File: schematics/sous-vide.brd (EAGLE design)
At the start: 81.3 x 81.3 mm, 32 parts, among them IC1 MEGA8-P, T1 BC547, T2 BC547, T3 BC547

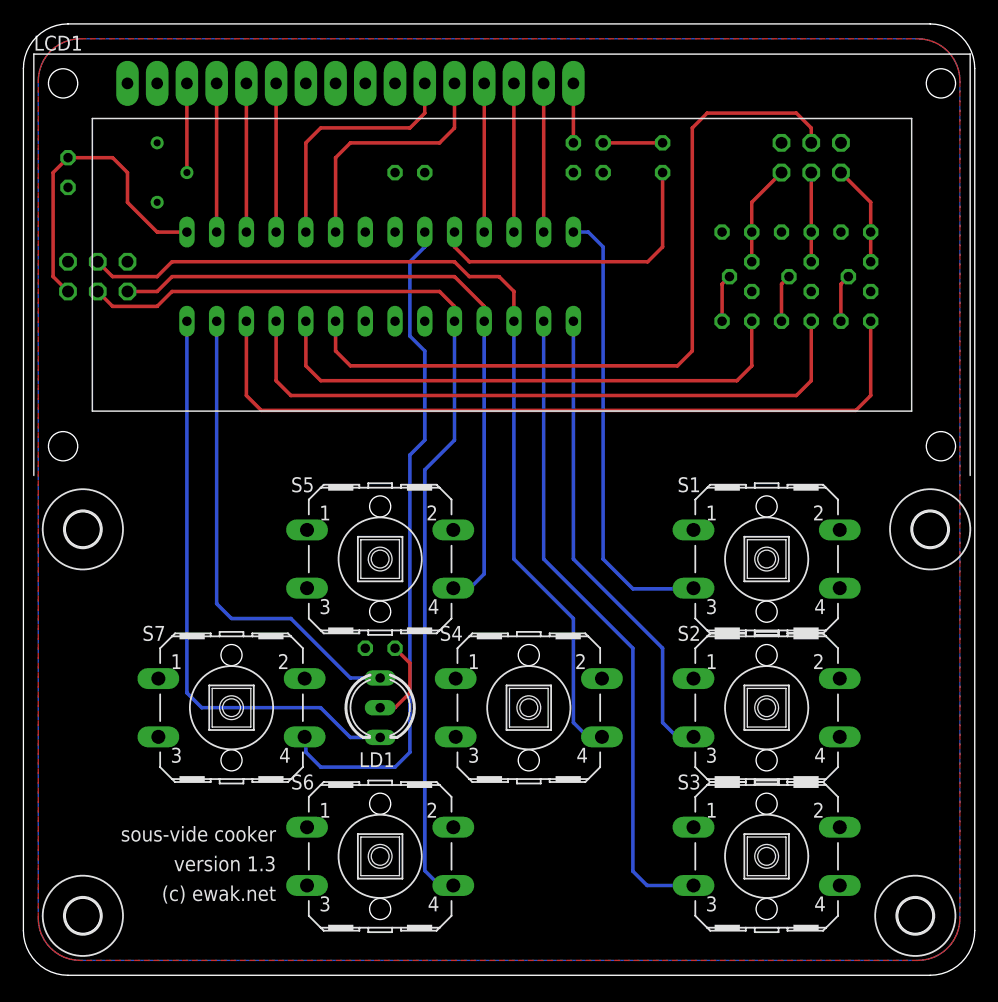
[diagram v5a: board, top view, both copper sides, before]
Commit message: Removed button and LED and added crystal for more precise timing over longer periods.
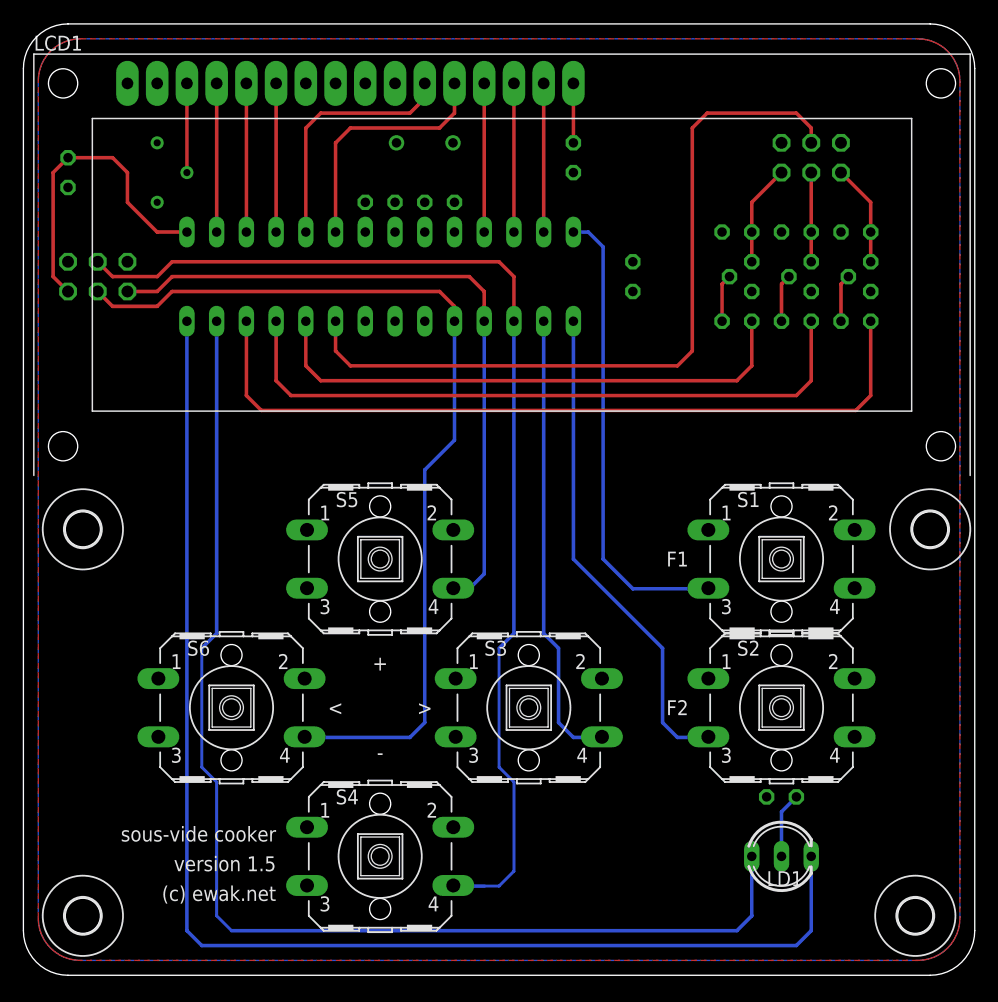
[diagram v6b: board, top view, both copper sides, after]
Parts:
- removed LED1: (no value), led:LED3MM
- removed R8: 180, rcl:0207/2V
- removed S7: (no value), switch-omron:B3F-40XX
- added C2, C3: 100n, resistor:C025-025X050
- added Q1: (no value), crystal:HC49U-V
- moved LD1 36.6 mm to (64.8, 10.2), turned to 0 degrees
- moved R7 36.6 mm to (64.8, 15.2)
- moved S3 24.0 mm to (43.2, 22.9)
- moved S4 18.0 mm to (30.5, 10.2)
- moved S6 18.0 mm to (17.8, 22.9)
- moved C1 3.59 mm to (30.5, 66.0), turned to 180 degrees
- moved S1 1.27 mm to (64.8, 35.6)
- moved S2 1.27 mm to (64.8, 22.9)
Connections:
- removed net N$26: IC1.9, S7.4
- net GND: now also C1.1, C2.1, C3.2; no longer C1.2, R8.1, S7.1, S7.2
- net N$1: now also C1.2, IC1.9, Q1.2; no longer LED1.K, R8.2
- net N$15: now also C2.2, Q1.1; no longer LED1.A
- net N$35: now also S3.4; no longer S3.3
- net VCC: now also C3.1; no longer C1.1
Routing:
- net N$8: track 49.8 -> 112.8 mm
- net N$9: track 40.7 -> 103.7 mm
- net N$26: track 57.3 -> 0.00 mm
- net N$15: track 26.5 -> 0.00 mm
- net N$35: track 55.8 -> 39.1 mm
- net N$24: track 79.6 -> 94.6 mm
- net N$1: track 5.08 -> 0.00 mm
- net N$18: track 83.1 -> 79.6 mm
- net N$19: track 58.0 -> 60.1 mm
- net N$7: track 7.40 -> 5.61 mm
- net N$37: track 40.6 -> 41.9 mm
- net N$36: track 38.5 -> 39.8 mm
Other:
- board text added: "+"
- board text added: "+S-"
- board text added: "-"
- board text added: "<"
- board text added: ">"
- board text added: "CONTRAST"
- board text added: "F1"
- board text added: "F2"
- board text added: "ISP"
- board text added: "PHC"
- board text added: "version 1.5"
- board text removed: "version 1.3"

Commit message: PCB button and connector layout rearranged. NOT COMPATIBEL WITH PRE-1.5 CODE.
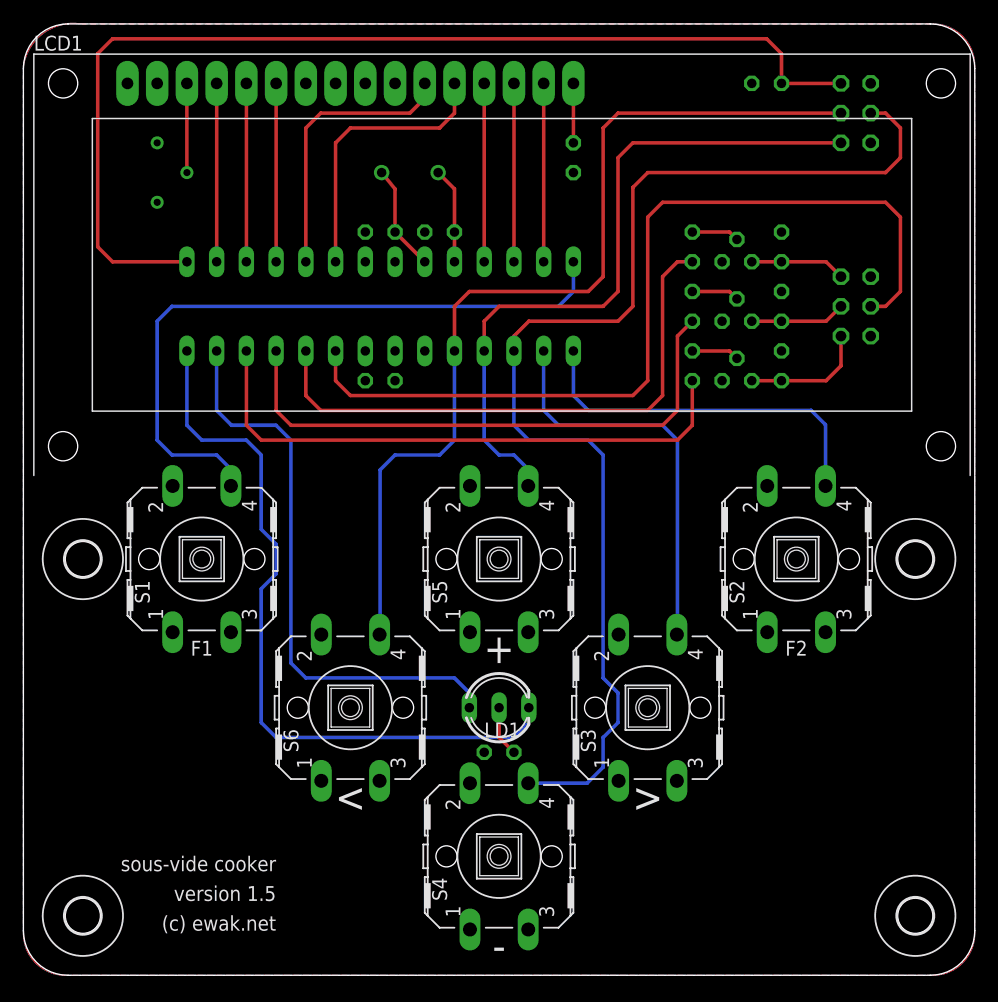
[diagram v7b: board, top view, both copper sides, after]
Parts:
- JP1, JP2: device pinhead:2X03 -> con-ml:ML6
- moved JP2 66.3 mm to (71.1, 73.7), turned to 90 degrees
- moved R1 60.2 mm to (63.5, 76.2), turned to 180 degrees
- moved S1 49.5 mm to (15.2, 35.6), turned to 90 degrees
- moved LD1 27.3 mm to (40.6, 22.9)
- moved R7 24.4 mm to (40.6, 19.1)
- moved C3 23.3 mm to (30.5, 50.8), turned to 0 degrees
- moved R4 14.5 mm to (57.1, 52.1), turned to 90 degrees
- moved T3 14.5 mm to (61.0, 50.8), turned to 0 degrees
- moved JP1 13.3 mm to (71.1, 57.1), turned to 90 degrees
- moved D3 13.1 mm to (64.8, 52.1), turned to 270 degrees
- moved S2 12.8 mm to (66.0, 35.6), turned to 90 degrees
- moved S3 10.2 mm to (53.3, 22.9), turned to 90 degrees
- moved S4 10.2 mm to (40.6, 10.2), turned to 90 degrees
- moved S5 10.2 mm to (40.6, 35.6), turned to 90 degrees
- moved S6 10.2 mm to (27.9, 22.9), turned to 90 degrees
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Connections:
- net N$36: now also S1.4; no longer S1.3
- net N$37: now also S2.4; no longer S2.3
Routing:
- net N$31: track 26.8 -> 91.7 mm
- net N$9: track 103.7 -> 49.1 mm
- net N$8: track 112.8 -> 62.8 mm
- net N$36: track 39.8 -> 58.1 mm
- net N$6: track 67.1 -> 49.3 mm
- net N$3: track 65.6 -> 76.3 mm
- net N$37: track 41.9 -> 31.6 mm
- net N$1: track 0.00 -> 9.08 mm
- net N$5: track 56.9 -> 48.6 mm
- net N$15: track 0.00 -> 8.20 mm
- net N$24: track 94.6 -> 101.9 mm
- net N$35: track 39.1 -> 34.2 mm
- net N$34: track 12.7 -> 15.2 mm
- net N$33: track 12.7 -> 15.2 mm
- net N$32: track 12.7 -> 15.2 mm
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
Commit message: Optimized traces and button definitions and send to pcb production as version 1.5
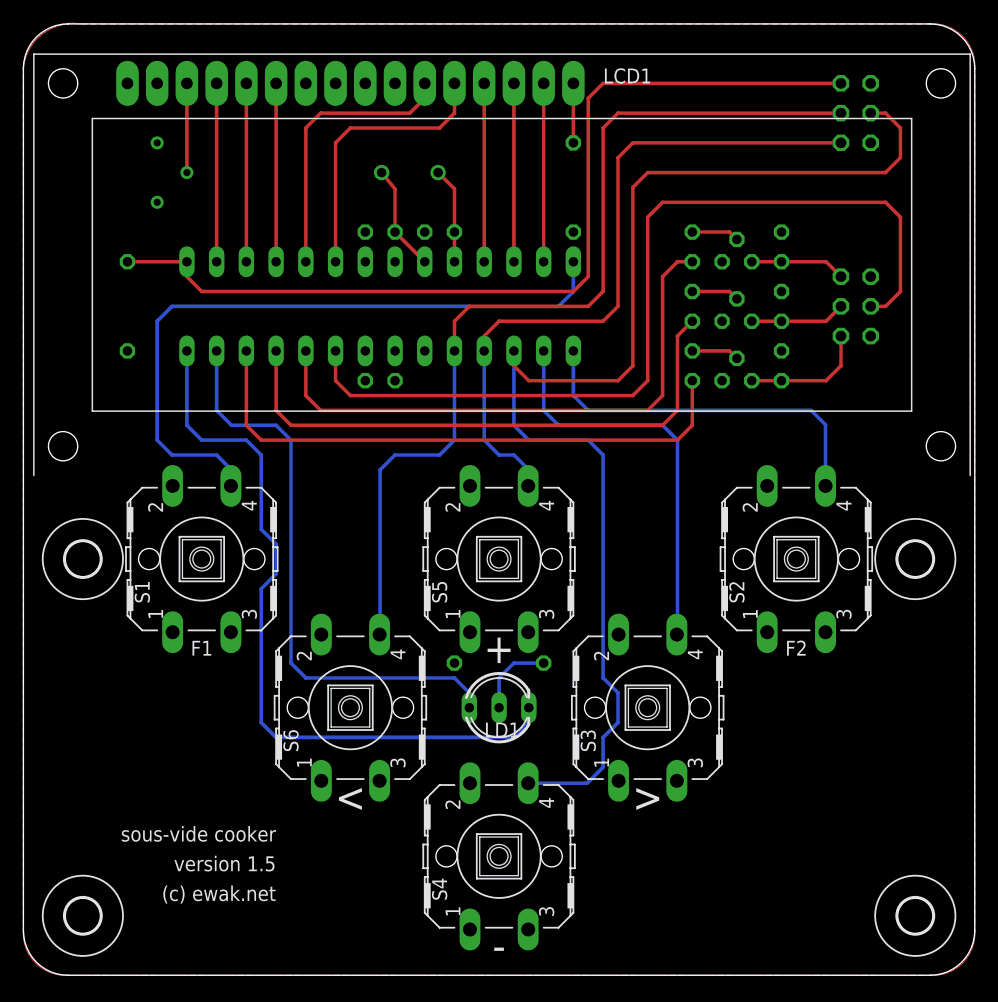
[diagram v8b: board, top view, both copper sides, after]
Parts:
- C1, C2: value 100n -> 22p
- R1, R6, R7: device rcl:0207/2V -> rcl:0207/7
- moved R1 57.8 mm to (8.89, 57.1), turned to 90 degrees
- moved R7 7.62 mm to (40.6, 26.7)
- moved R6 2.54 mm to (47.0, 67.3)
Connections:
- net GND: now also LCD1.10, LCD1.7, LCD1.8, LCD1.9
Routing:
- net N$31: track 91.7 -> 79.0 mm
- net N$24: track 101.9 -> 107.0 mm
- net N$7: track 4.34 -> 6.88 mm
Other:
- board text added: "IO"
